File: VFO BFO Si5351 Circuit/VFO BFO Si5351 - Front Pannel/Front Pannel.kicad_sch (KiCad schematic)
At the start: 22 parts, among them J1 LED, J2 Optical Rotary Encoder, J3 Mecc_rotary encoder, J4 VFO_Front_Pannel, SW1 RotaryEncoder_Clarifier, SW2 SW_Band, SW3 SW_Mode, SW4 SW_AGC, SW5 SW_ATT, SW6 SW_Scan, SW7 SW_Step, SW8 SW_RTTY_CW, U1 Ili9341_Module_TFT_320x240_To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

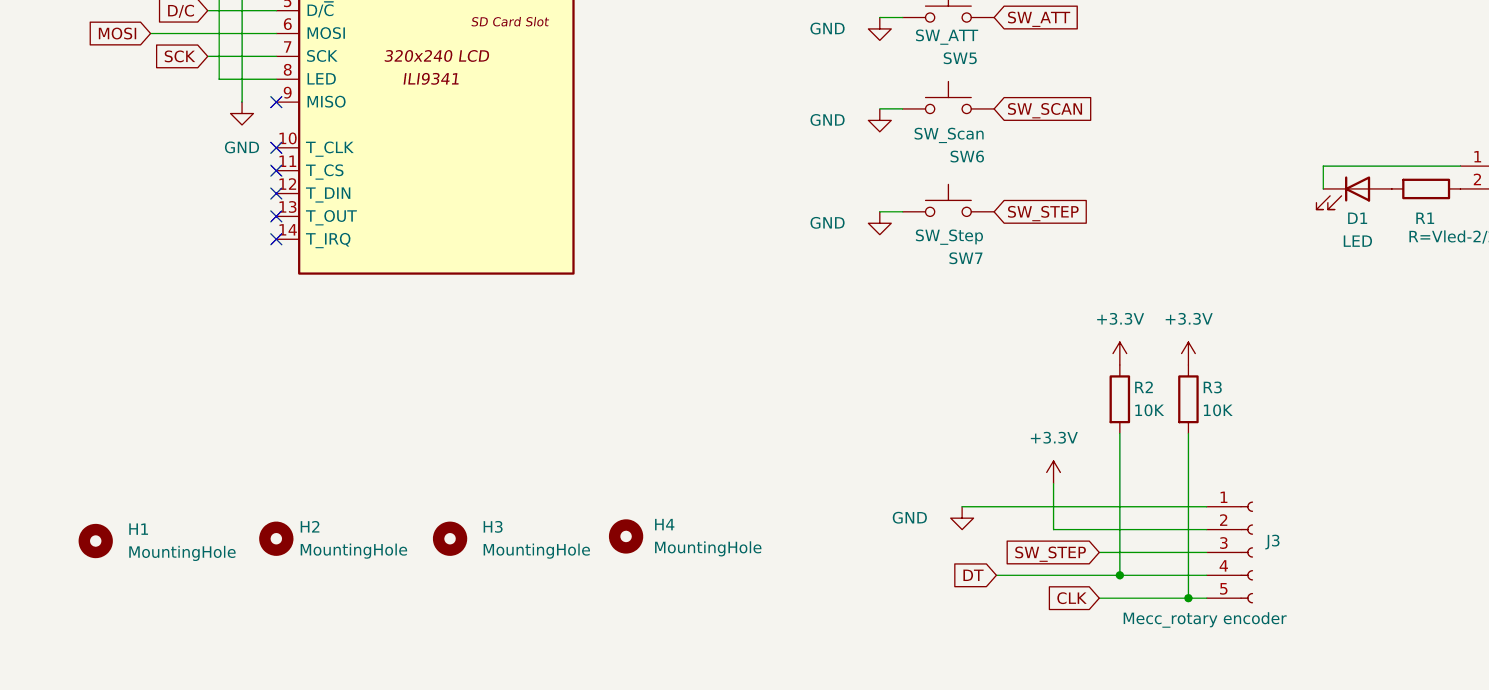
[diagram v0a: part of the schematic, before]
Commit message: PDF distenta componenti e  schemi elettrico e di montaggio
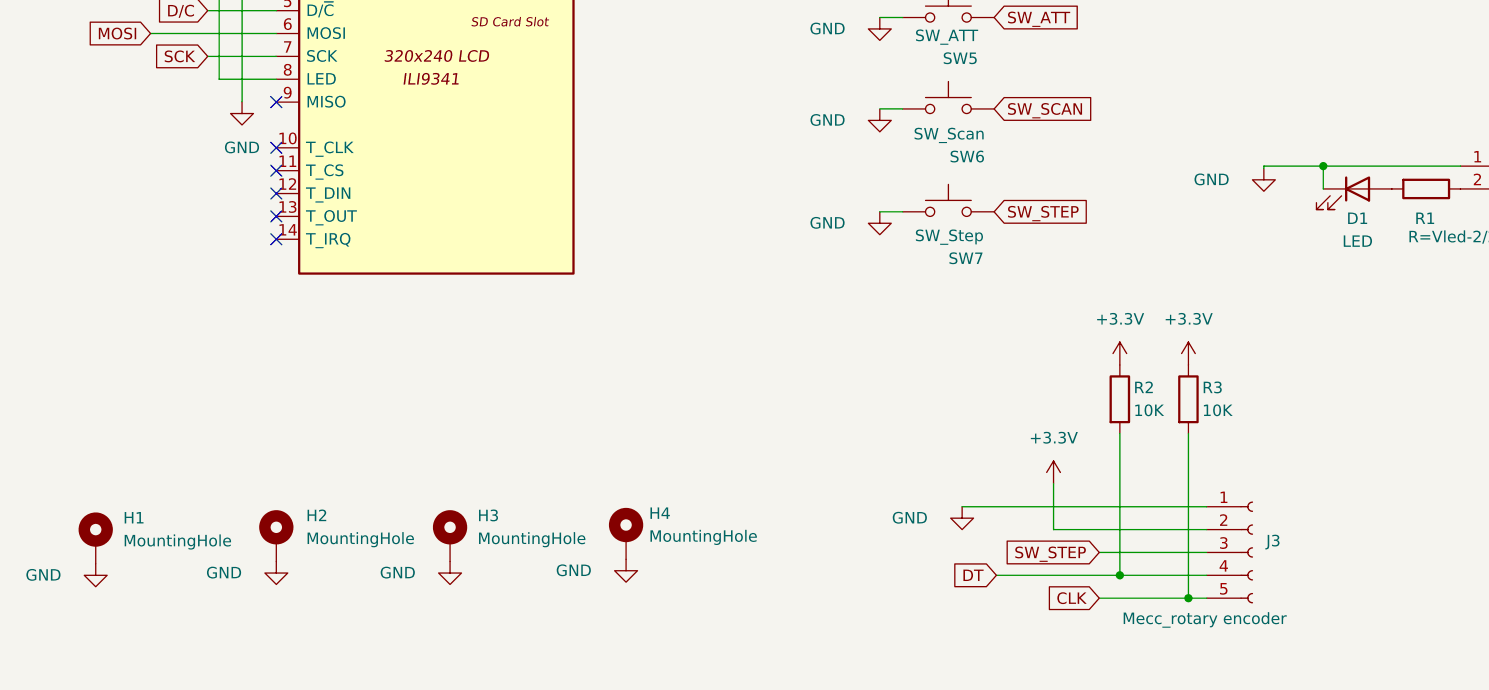
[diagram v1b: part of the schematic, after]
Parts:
- H1, H2, H3, H4: footprint MountingHole:MountingHole_3.2mm_M3_DIN965 -> MountingHole:MountingHole_3.2mm_M3_DIN965_Pad_TopBottom; symbol Mechanical:MountingHole -> Mechanical:MountingHole_Pad
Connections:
- net GND: now also D1.1 (K), H1.1, H2.1, H3.1, H4.1, J1.1 (Pin_1)
